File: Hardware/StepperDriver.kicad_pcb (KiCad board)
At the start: 4 copper layers, 0 parts

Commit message: Initial schematic
Completed the first iteration for the schematic.
Included a default 42x42mm PCB area.
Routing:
- added copper zone on B.Cu, net GND
- added copper zone on F.Cu, net GND
- added copper zone on In1.Cu, net GND
- added copper zone on In2.Cu, net GND
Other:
- board outline added: 42 x 42 mm
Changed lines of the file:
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@@
 		(filling no)
 		(zone_defaults)
+		(aux_axis_origin 150 100)
+		(grid_origin 150 100)
 		(pcbplotparams
 			(layerselection 0x00000000_00000000_55555555_5755f5ff)
@@
 		)
 	)
+	(gr_rect
+		(start 129 79)
+		(end 171 121)
+		(stroke
+			(width 0.05)
+			(type solid)
+		)
+		(fill no)
+		(layer "Edge.Cuts")
+	)
+	(zone
+		(net "GND")
+		(layers "F.Cu" "B.Cu" "In1.Cu" "In2.Cu")
+		(hatch edge 0.5)
+		(connect_pads
+			(clearance 0.5)
+		)
+		(min_thickness 0.25)
+		(fill yes
+			(thermal_gap 0.5)
+			(thermal_bridge_width 0.5)
+			(island_removal_mode 0)
+		)
+		(polygon
+			(pts
+				(xy 110 65) (xy 190 65) (xy 190 140) (xy 110 140)
+			)
+		)
+	)

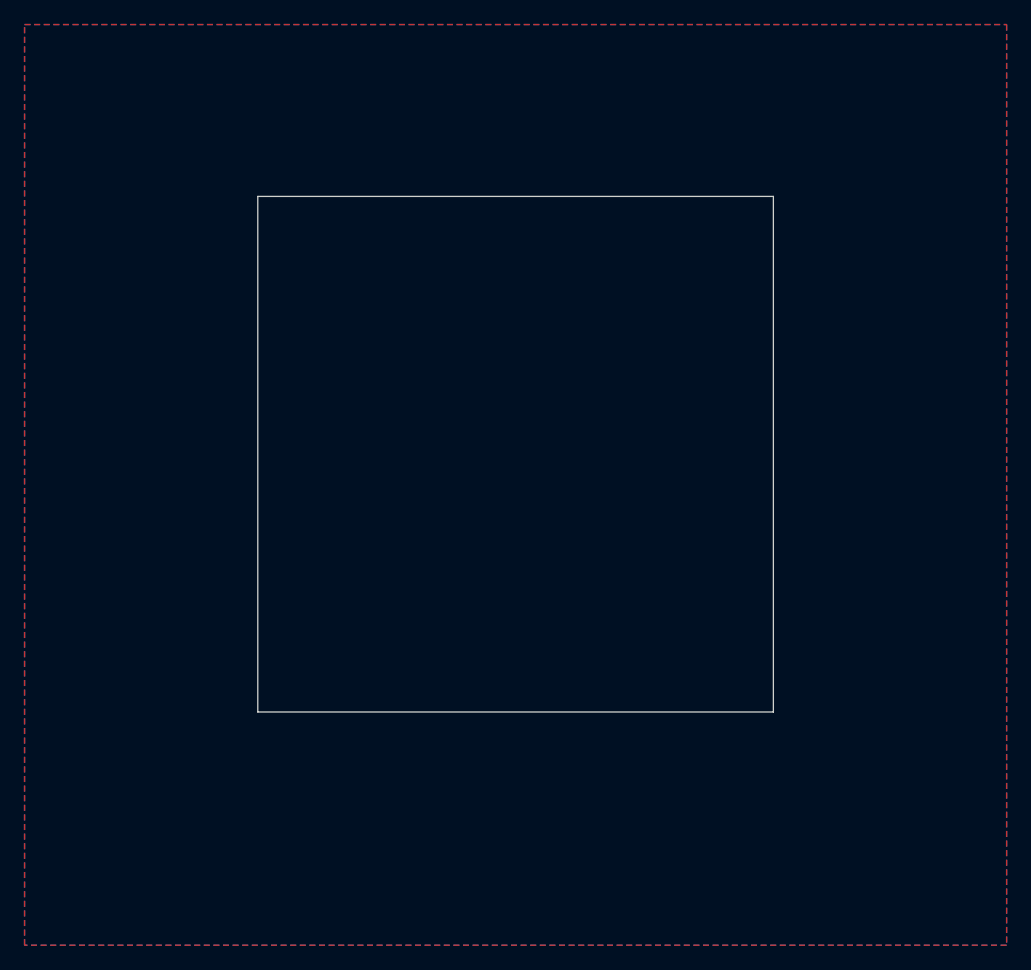
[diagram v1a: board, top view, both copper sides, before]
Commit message: Initial layout
Completed the first iteration for the layout.
Increased the PCB area to 50x50mm.
Minor changes in the schematic.
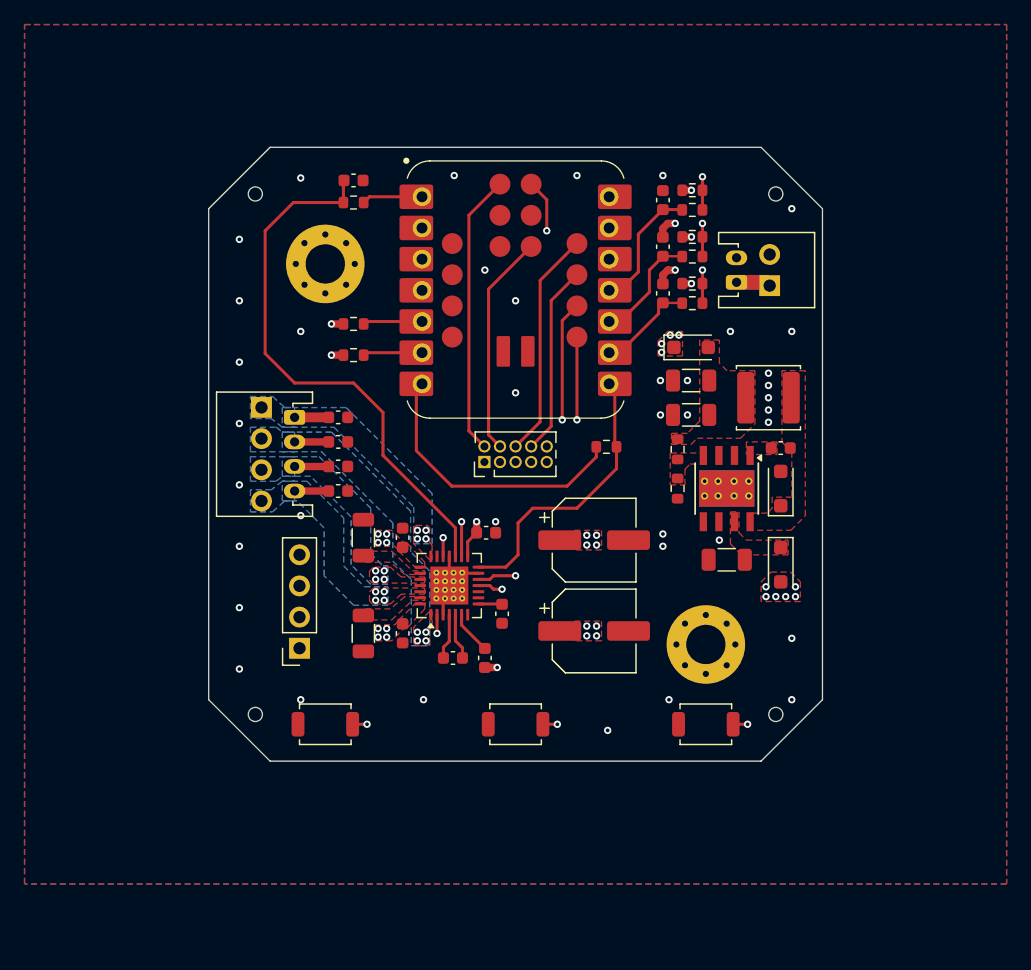
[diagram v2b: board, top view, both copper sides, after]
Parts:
- added C1: 100n, Capacitor_SMD:C_0603_1608Metric, F.Cu at (147.6, 106.4)
- added C10: 22u, Capacitor_SMD:C_1206_3216Metric, F.Cu at (164.3, 94.0)
- added C11: 22n, Capacitor_SMD:C_0603_1608Metric, F.Cu at (144.9, 116.6)
- added C12: 100n, Capacitor_SMD:C_0603_1608Metric, F.Cu at (135.6, 103.0)
- added C13: 100n, Capacitor_SMD:C_0603_1608Metric, F.Cu at (135.6, 101.0)
- added C14: 100n, Capacitor_SMD:C_0603_1608Metric, F.Cu at (135.6, 99.0)
- added C15: 100n, Capacitor_SMD:C_0603_1608Metric, F.Cu at (135.6, 97.0)
- added C16: 2.2u, Capacitor_SMD:C_0603_1608Metric, F.Cu at (148.9, 113.0)
- added C17: 1u, Capacitor_SMD:C_0603_1608Metric, F.Cu at (136.8, 77.7)
- added C18: 10n, Capacitor_SMD:C_0603_1608Metric, F.Cu at (162.0, 79.3)
- added C19: 10n, Capacitor_SMD:C_0603_1608Metric, F.Cu at (162.0, 83.1)
- added C2: 100n, Capacitor_SMD:C_0603_1608Metric, F.Cu at (140.8, 114.6)
- added C20: 10n, Capacitor_SMD:C_0603_1608Metric, F.Cu at (162.0, 86.9)
- added C3: 100n, Capacitor_SMD:C_0603_1608Metric, F.Cu at (140.8, 106.8)
- added C4: 47u, Capacitor_SMD:CP_Elec_6.3x5.4, F.Cu at (156.4, 107.0)
- added C5: 47u, Capacitor_SMD:CP_Elec_6.3x5.4, F.Cu at (156.4, 114.4)
- added C6: 10n, Capacitor_SMD:C_0603_1608Metric, F.Cu at (171.6, 99.5)
- added C7: 22u, Capacitor_SMD:C_1206_3216Metric, F.Cu at (167.2, 108.6)
- added C8: 100n, Capacitor_SMD:C_0603_1608Metric, F.Cu at (147.5, 116.6)
- added C9: 22u, Capacitor_SMD:C_1206_3216Metric, F.Cu at (164.3, 96.8)
- added D1: DSK24, Diode_SMD:D_SOD-123F, F.Cu at (171.6, 109.0)
- added D2: DSK24, Diode_SMD:D_SOD-123F, F.Cu at (164.3, 91.3)
- added D3: DSK24, Diode_SMD:D_SOD-123F, F.Cu at (171.6, 102.8)
- added H1: MOUNT, MountingHole:MountingHole_3.2mm_M3_Pad_Via, F.Cu at (134.5, 84.5)
- added H2: MOUNT, MountingHole:MountingHole_3.2mm_M3_Pad_Via, F.Cu at (165.5, 115.5)
- added H3: TOOL, MountingHole:ToolingHole_1.152mm, F.Cu at (128.8, 78.8)
- added H4: TOOL, MountingHole:ToolingHole_1.152mm, F.Cu at (171.2, 78.8)
- added H5: TOOL, MountingHole:ToolingHole_1.152mm, F.Cu at (171.2, 121.2)
- added H6: TOOL, MountingHole:ToolingHole_1.152mm, F.Cu at (128.8, 121.2)
- added J1: DC, Custom_Parts:JST_PH_S2B_1x02_COMBO, F.Cu at (168.0, 86.0)
- added J2: MOTOR, Custom_Parts:JST_PH_S4B_1x04_COMBO, F.Cu at (132.0, 97.0)
- added J3: OLED, Custom_Parts:OLED_128X32_0.91_HEADER, F.Cu at (132.4, 115.8)
- added J4: JTAG, Connector_PinHeader_1.27mm:PinHeader_2x05_P1.27mm_Vertical, F.Cu at (147.5, 100.6)
- added L1: 100u, Inductor_SMD:L_Changjiang_FNR5040S, F.Cu at (170.6, 95.4)
- added R1: 10K, Resistor_SMD:R_0603_1608Metric, F.Cu at (163.2, 99.6)
- added R10: 10K, Resistor_SMD:R_0603_1608Metric, F.Cu at (164.4, 82.3)
- added R11: 10K, Resistor_SMD:R_0603_1608Metric, F.Cu at (164.4, 86.1)
- added R12: 10K, Resistor_SMD:R_0603_1608Metric, F.Cu at (164.4, 80.1)
- added R13: 10K, Resistor_SMD:R_0603_1608Metric, F.Cu at (164.4, 83.9)
- added R14: 10K, Resistor_SMD:R_0603_1608Metric, F.Cu at (164.4, 87.7)
- added R2: 3.3K, Resistor_SMD:R_0603_1608Metric, F.Cu at (163.2, 102.8)
- added R3: 22K, Resistor_SMD:R_0603_1608Metric, F.Cu at (136.8, 79.5)
- added R4: 100m, Resistor_SMD:R_1206_3216Metric, F.Cu at (137.6, 106.8)
- added R5: 100m, Resistor_SMD:R_1206_3216Metric, F.Cu at (137.6, 114.6)
- added R6: 2.2K, Resistor_SMD:R_0603_1608Metric, F.Cu at (136.8, 91.9)
- added R7: 2.2K, Resistor_SMD:R_0603_1608Metric, F.Cu at (136.8, 89.4)
- added R8: 1K, Resistor_SMD:R_0603_1608Metric, F.Cu at (157.4, 99.4)
- added R9: 10K, Resistor_SMD:R_0603_1608Metric, F.Cu at (164.4, 78.5)
- added SW1: SW_M, Button_Switch_SMD:SW_SPST_TS-1088-xR020, F.Cu at (134.5, 122.0)
- added SW2: SW_C, Button_Switch_SMD:SW_SPST_TS-1088-xR020, F.Cu at (150.0, 122.0)
- added SW3: SW_P, Button_Switch_SMD:SW_SPST_TS-1088-xR020, F.Cu at (165.5, 122.0)
- added U1: TPS5430DDA, Custom_Parts:TI_SO-PowerPAD-8_ThermalVias, F.Cu at (167.2, 102.8)
- added U2: TMC2208-LA, Custom_Parts:QFN-28-1EP_5x5mm_P0.5mm_EP3.1x3.1mm_ThermalVias, F.Cu at (144.6, 110.7)
- added U3: XIAO-RP2350, Custom_Parts:XIAO-RP2350-SMD, F.Cu at (150.0, 86.7)
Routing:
- net /SW_RAWM: track 0.00 -> 67.8 mm, vias 0 -> 2
- net /SW_RAWC: track 0.00 -> 50.3 mm, vias 0 -> 2
- net /SW_RAWP: track 0.00 -> 45.2 mm, vias 0 -> 2
- net /VREF: track 0.00 -> 44.8 mm
- net /DRV_EN: track 0.00 -> 32.1 mm, vias 0 -> 1
- net /DRV_STEP: track 0.00 -> 28.4 mm, vias 0 -> 1
- net /SDA: track 0.00 -> 27.2 mm
- net /SCL: track 0.00 -> 27.2 mm
- net /DRV_INDEX: track 0.00 -> 27.2 mm, vias 0 -> 2
- net /DRV_DIAG: track 0.00 -> 26.2 mm, vias 0 -> 2
- net /DRV_DIR: track 0.00 -> 25.5 mm, vias 0 -> 1
- net /TX: track 0.00 -> 23.1 mm
- net /SWDIO: track 0.00 -> 22.9 mm
- net /DRV_UART: track 0.00 -> 22.9 mm
- net /RST: track 0.00 -> 21.9 mm, vias 0 -> 1
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- added copper zone on In2.Cu, net +3V3
- added copper zone on F.Cu, net +5V
- added copper zone on In2.Cu, net +5V
- added copper zone on F.Cu, net +VDC
- added copper zone on In2.Cu, net +VDC
- added copper zone on F.Cu, net /5V_RAW
- added copper zone on F.Cu, net /BOOT
- added copper zone on B.Cu, net /M_A1
- added copper zone on F.Cu, net /M_A1
- added copper zone on B.Cu, net /M_A2
- added copper zone on F.Cu, net /M_A2
- added copper zone on B.Cu, net /M_B1
- added copper zone on F.Cu, net /M_B1
- added copper zone on B.Cu, net /M_B2
- added copper zone on F.Cu, net /M_B2
- added copper zone on F.Cu, net /SNSA
- added copper zone on F.Cu, net /SNSB
- added copper zone on F.Cu, net /VDC_PROT
- added copper zone on F.Cu, net /VSNS
- added copper zone on F.Cu, net /VSW
- added copper zone on In4.Cu, net GND
- removed copper zone on In2.Cu, net GND
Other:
- board size 42 x 42 mm -> 50 x 50 mm
- copper layers 4 -> 6

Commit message: Initial ESP32C6 layout
Moved to a XIAO ESP32C6 development board.
Completed the first iteration for the layout.
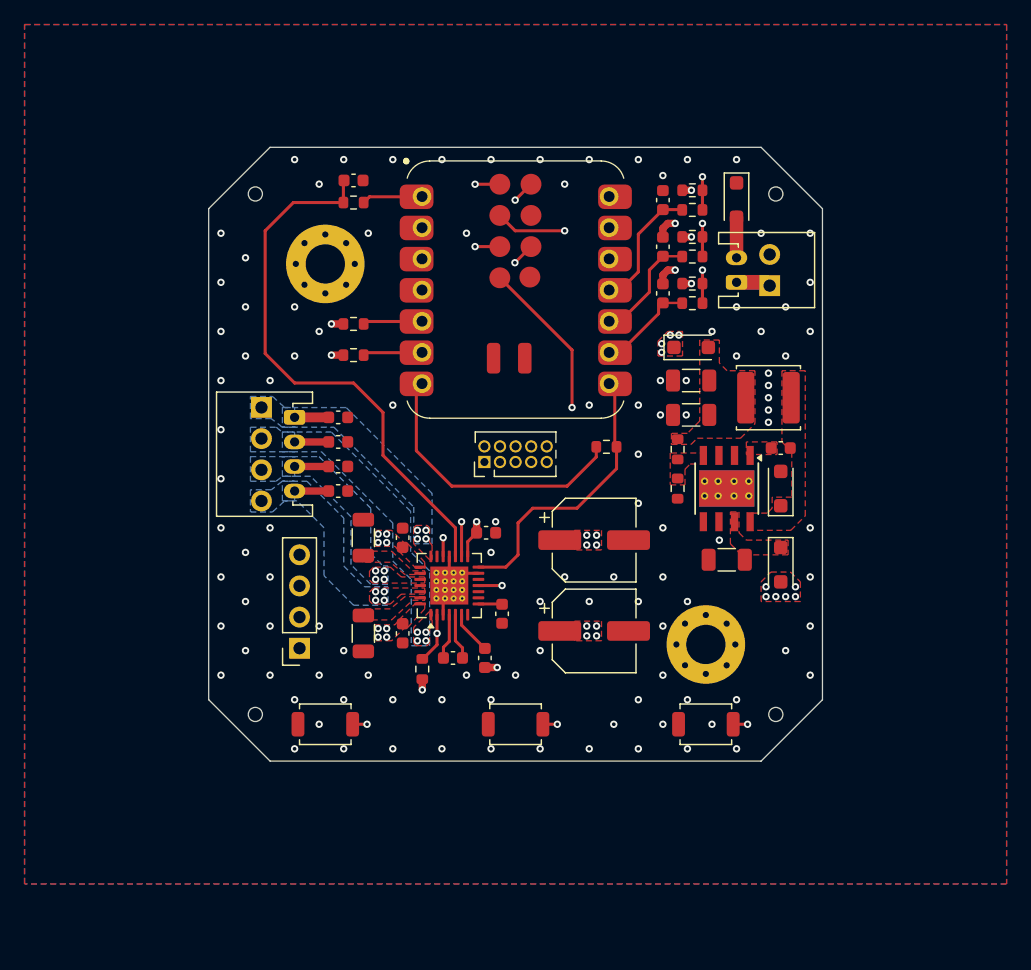
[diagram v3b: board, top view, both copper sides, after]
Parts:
- added D4: SMF40CA, Diode_SMD:D_SOD-123F, F.Cu at (168.0, 79.3)
- added R15: 10K, Resistor_SMD:R_0603_1608Metric, F.Cu at (142.4, 117.5)
- U3: value XIAO-RP2350 -> XIAO-ESP32C6; footprint Custom_Parts:XIAO-RP2350-SMD -> Custom_Parts:XIAO-ESP32C6-SMD
- moved H5 42.4 mm to (128.8, 121.2)
- moved H6 42.4 mm to (171.2, 121.2)
- turned U3 to 0 degrees
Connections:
- J4 pad 2: /SWDIO -> /TMS
- J4 pad 4: /SWCLK -> /TCK
- J4 pad 6: /UART_RX -> /TDO
- J4 pad 8: /UART_TX -> /TDI
- U2 pad 12: /DRV_INDEX -> unconnected-(U2-INDEX-Pad12)
- U3 pad 15: /UART_RX -> /TDI
- U3 pad 16: /UART_TX -> /TDO
- U3 pad 17: /DRV_INDEX -> /RST
- U3 pad 18: /DRV_DIAG -> GND
- U3 pad 19: unconnected-(U3-GPIO11_SPI1_MOSI-Pad19) -> /TMS
- U3 pad 20: unconnected-(U3-GPIO12_SPI1_MISO-Pad20) -> /TCK
- U3 pad 21: unconnected-(U3-GPIO10_SPI1_SCK-Pad21) -> /DRV_DIAG
- U3 pad 23: /SWDIO -> unconnected-(U3-BAT-Pad23)
- U3 pad 24: /RST -> GND
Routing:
- net /TDI: track 0.00 -> 28.8 mm, vias 0 -> 1
- net /DRV_INDEX: track 27.2 -> 0.00 mm, vias 2 -> 0
- net /TDO: track 0.00 -> 23.2 mm, vias 0 -> 1
- net /SWDIO: track 22.9 -> 0.00 mm
- net /TMS: track 0.00 -> 18.6 mm, vias 0 -> 1
- net /UART_RX: track 18.6 -> 0.00 mm
- net /SWCLK: track 18.1 -> 0.00 mm
- net /TCK: track 0.00 -> 17.3 mm, vias 0 -> 1
- net /UART_TX: track 15.5 -> 0.00 mm
- net /DRV_DIAG: track 26.2 -> 31.8 mm
- net +VDC: track 1.00 -> 4.30 mm
- net /DRV_EN: track 32.1 -> 34.7 mm
- net /RST: track 21.9 -> 24.0 mm
- net +3V3: track 7.33 -> 8.20 mm, vias 6 -> 7
- net GND: vias 41 -> 112

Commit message: Build output files
Generated the output files for the first iteration of the ESP32-C6 board.
Added some board images and 3D model.
Added the BOM and POS files for assembly.
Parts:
- added FID1: FIDUCIAL, Fiducial:Fiducial_0.75mm_Mask1.5mm, F.Cu at (127.5, 81.0)
- added FID2: FIDUCIAL, Fiducial:Fiducial_0.75mm_Mask1.5mm, F.Cu at (127.5, 119.0)
- added FID3: FIDUCIAL, Fiducial:Fiducial_0.75mm_Mask1.5mm, F.Cu at (172.5, 119.0)
- added REF**: MT, Logos:MT, B.Cu at (141.5, 113.9)
- C7: value 22u -> 10u
- J3: footprint Custom_Parts:OLED_128X32_0.91_HEADER -> Custom_Parts:HEADER_THROUGH_1x04_P2.54mm
- L1: value 100u -> 47u
- moved J3 3.81 mm to (132.4, 112.0), turned to 0 degrees
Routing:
- net /SDA: track 27.2 -> 29.6 mm, vias 0 -> 1
- net /SCL: track 27.2 -> 29.1 mm, vias 0 -> 1
- net +3V3: track 8.20 -> 9.75 mm, vias 7 -> 8
- net GND: vias 112 -> 109
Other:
- board text added: "3V3"
- board text added: "A1"
- board text added: "A2"
- board text added: "B1"
- board text added: "B2"
- board text added: "DAVID MT"
- board text added: "GND"
- board text added: "JTAG"
- board text added: "MOTOR"
- board text added: "PD 05/26"
- board text added: "POWER"
- board text added: "SCL"
- board text added: "SDA"
- board text added: "STEPPER DRIVER"
- board text added: "SW+"
- board text added: "SW-"
- board text added: "SWC"
- board text added: "V+"
- board text added: "V-"
- board text added: "V1.0 REV A"
- board text added: "XIAO ESP32C6"

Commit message: Assembly revision
Minor changes to the board and schematic.
Updated the output files.
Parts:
- SW1: value SW_M -> SPST_TS
- SW2: value SW_C -> SPST_TS
- SW3: value SW_P -> SPST_TS
- renumbered D4 to D3, D3 to D4, R9 to R10, R10 to R11, R11 to R12, R12 to R13, R13 to R14, R14 to R15, R15 to R3, R3 to R4, R4 to R5, R5 to R6, R6 to R7, R7 to R8, R8 to R9
